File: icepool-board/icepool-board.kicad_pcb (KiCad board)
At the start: 4 copper layers, 100 x 40 mm, 118 parts, among them J1 PWR, J2 PWR_IN, J3 I2C, J4 SWD, J5 8P8C_Shielded, J6 8P8C_Shielded, SW1 B3U-1000P, U1 LD1117S33CTR, U2 LD1117S12CTR, U3 ATSAMD21E, U4 ISL83488/ISL83490, U5 iCE40HX8K-BG121(121-Ball_caBG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, U6 iCE40HX8K-BG121(121-Ball_caBG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, X1 ASV-12.000MHz-L??-50, Y1 16MHz

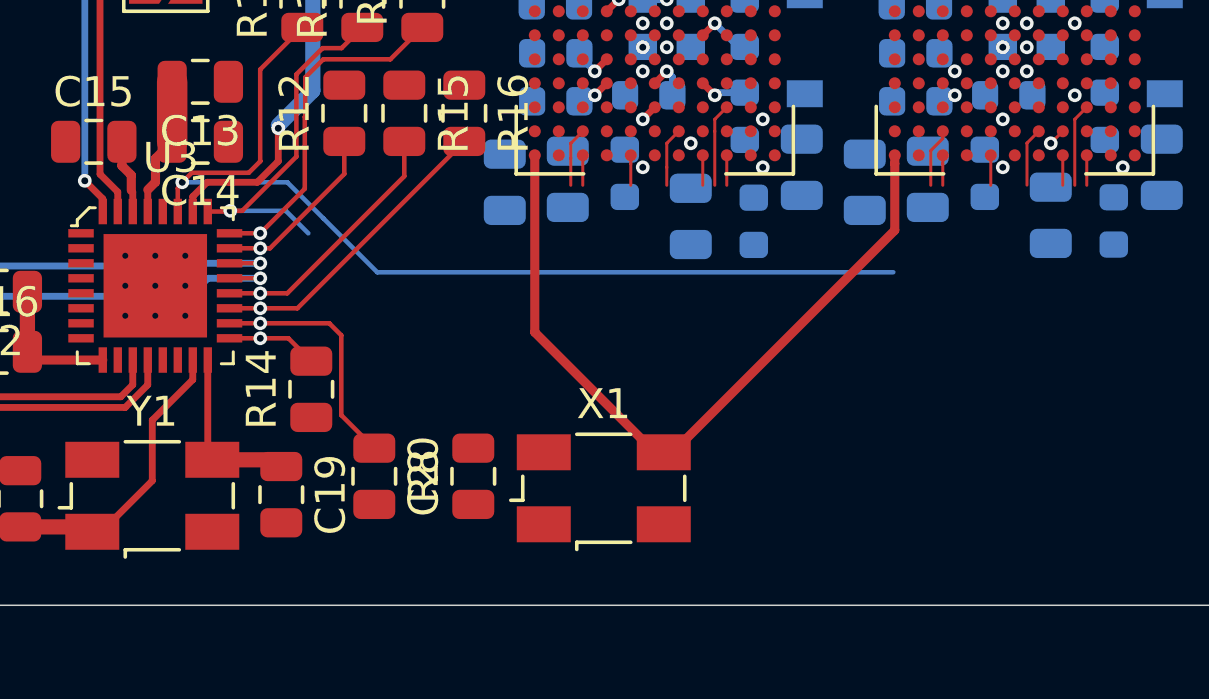
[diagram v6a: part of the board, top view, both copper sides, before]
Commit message: Reduced READY_ANY/READY_ALL to READY.
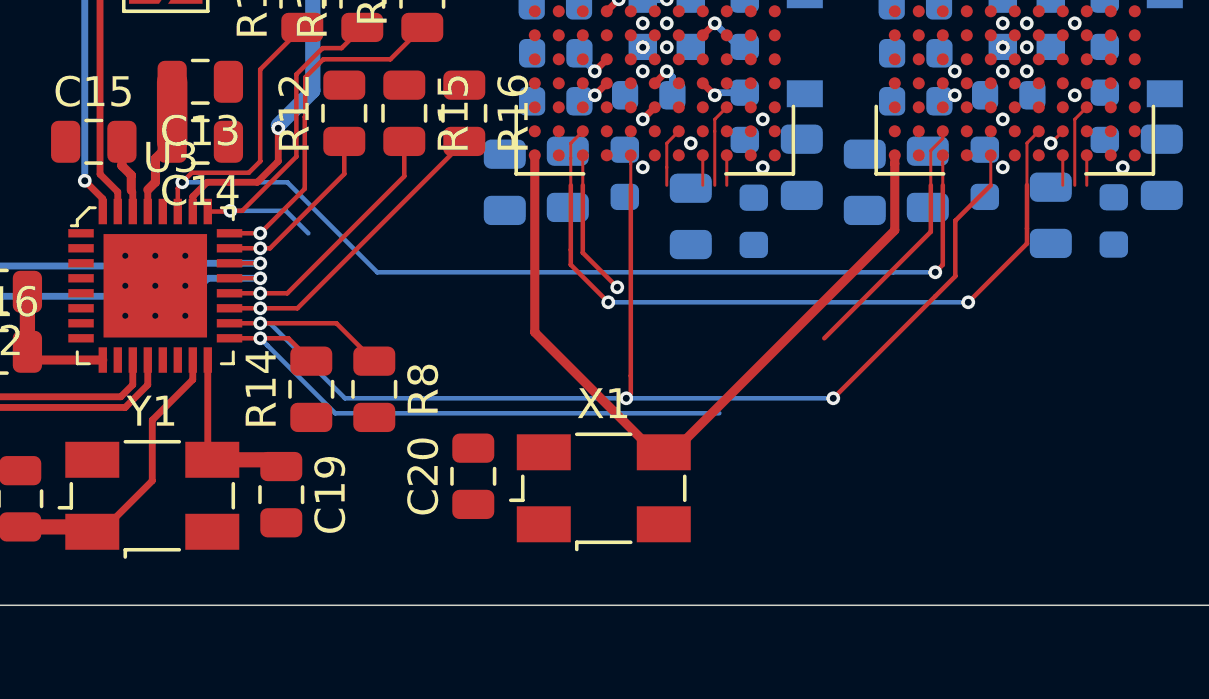
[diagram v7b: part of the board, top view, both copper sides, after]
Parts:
- moved R8 2.90 mm to (62.2, 112.8)
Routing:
- net /~WE: track 10.1 -> 43.9 mm, vias 1 -> 3
- net /FIFO_0_1: track 3.92 -> 25.1 mm, vias 0 -> 2
- net /MOSI: track 10.5 -> 26.9 mm
- net /MISO: track 10.6 -> 17.1 mm
- net /~READY_ALL: track 35.0 -> 39.4 mm, vias 1 -> 2
- net /~READY_ANY: track 13.2 -> 17.1 mm, vias 1 -> 2

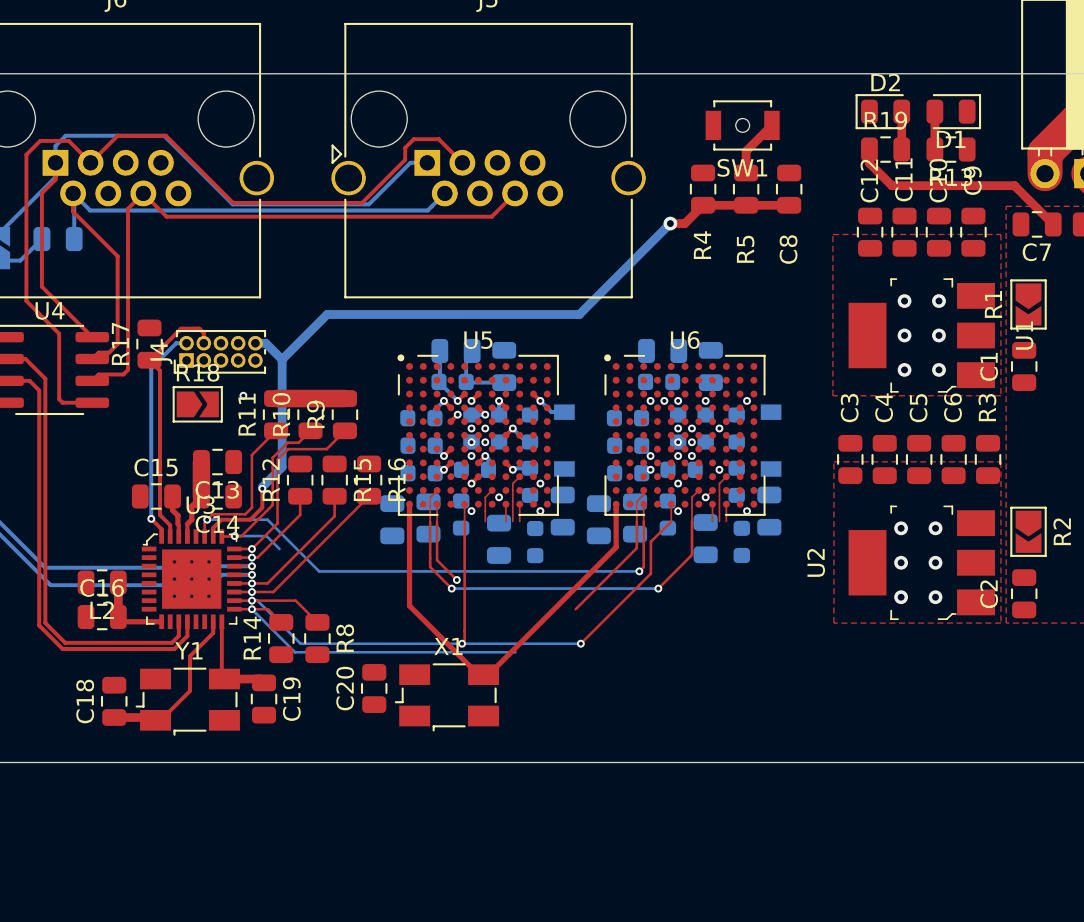
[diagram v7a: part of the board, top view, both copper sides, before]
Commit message: IO bus tracks laid.
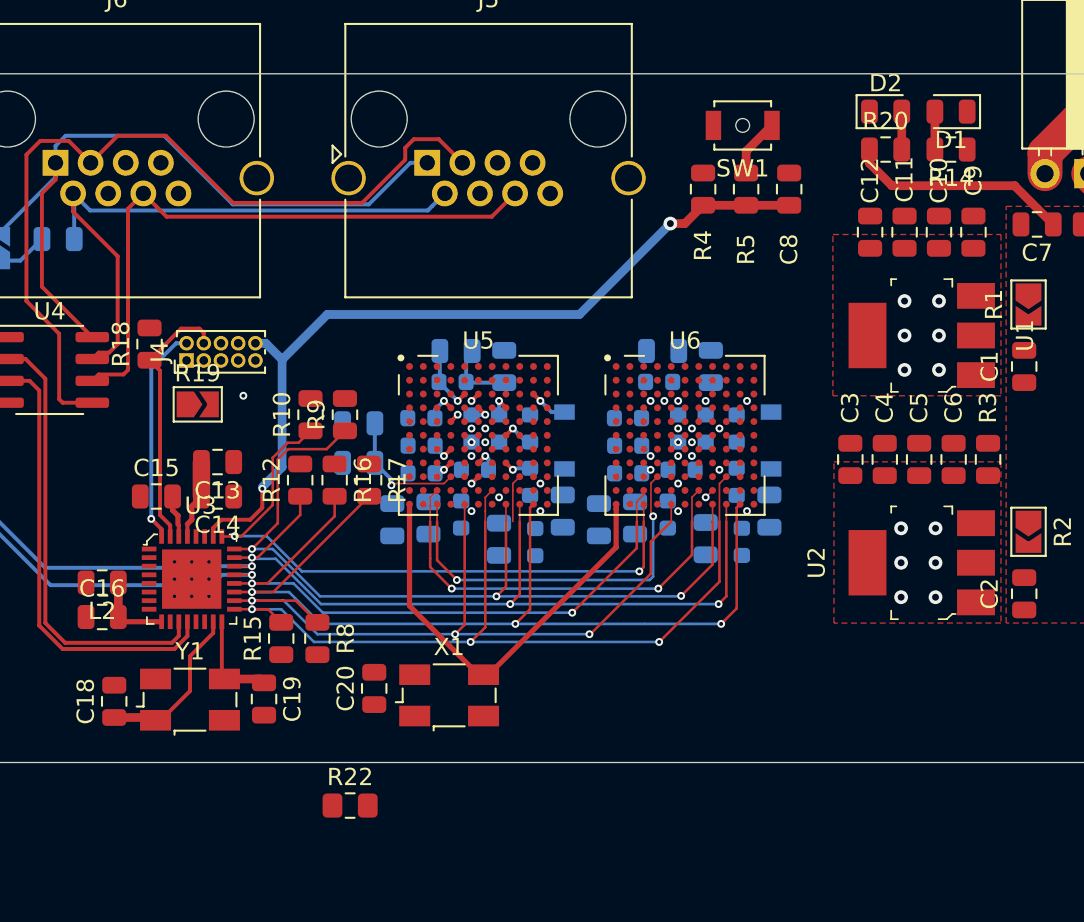
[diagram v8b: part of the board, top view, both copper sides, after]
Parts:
- removed the R15 at (63.2, 103.6)
- added R13: OMIT, Resistor_SMD:R_0805_2012Metric, B.Cu at (64.6, 100.3)
- added R16: 4k7, Resistor_SMD:R_0805_2012Metric, F.Cu at (63.2, 103.6)
- added R22: OMIT, Resistor_SMD:R_0805_2012Metric_Pad1.15x1.40mm_HandSolder, F.Cu at (64.1, 122.5)
- R10, R12, R4, R8, R9: value 10k -> 4k7
- R11: value 10k -> 4k7; moved to B.Cu
- R15: renamed from R14; value 10k -> 4k7
- R17: renamed from R16; value 10k -> 4k7
- moved R11 5.56 mm to (64.6, 102.6), turned to 180 degrees
- renumbered R13 to R14, R17 to R18, R18 to R19, R19 to R20, R20 to R21, R22 to R23, R23 to R24, R24 to R25, R25 to R26, R26 to R27, R27 to R28, R28 to R29, R29 to R30
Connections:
- R10 pad 1: /~READY_ANY -> /READY
- R11 pad 1: /~READY_ALL -> /READY_0
- U3 pad 25: /~READY_ANY -> /READY
- U3 pad 27: /~READY_ALL -> Net-(U3-Pad27)
- U5 pad J4: GND -> /READY_0
- U5 pad L3: /~READY_ANY -> /READY_0_1
- U6 pad J4: /~READY_ANY -> /READY_0_1
- U6 pad L3: /~READY_ALL -> /READY
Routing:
- net /SCK: track 10.1 -> 52.9 mm, vias 1 -> 3
- net /~READY_ALL: track 39.4 -> 0.00 mm, vias 2 -> 0
- net /CRESET_B: track 7.94 -> 46.2 mm, vias 1 -> 3
- net /READY: track 0.00 -> 37.7 mm, vias 0 -> 2
- net /~GS: track 13.4 -> 49.2 mm, vias 1 -> 3
- net /MOSI: track 26.9 -> 50.8 mm, vias 1 -> 3
- net /READY_0_1: track 0.00 -> 22.4 mm, vias 0 -> 2
- net /MISO: track 17.1 -> 36.7 mm, vias 1 -> 2
- net /~READY_ANY: track 17.1 -> 0.00 mm, vias 2 -> 0
- net /READY_0: track 0.00 -> 7.66 mm, vias 0 -> 1
- net +3V3: track 13.3 -> 9.30 mm
- net /~WE: track 43.9 -> 43.4 mm
